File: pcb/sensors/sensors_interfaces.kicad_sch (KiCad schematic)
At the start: 23 parts, among them J3 CAN BUS, J4 DIMMER I2C, J5 DIMMER I2C, J6 FLOW HALL, J7 VALVE SSR, J8 BOILER SSR, Q2 AO3401A, Q3 2N7002, U4 TJA1051T/3, U5 TMP102AIDRLR

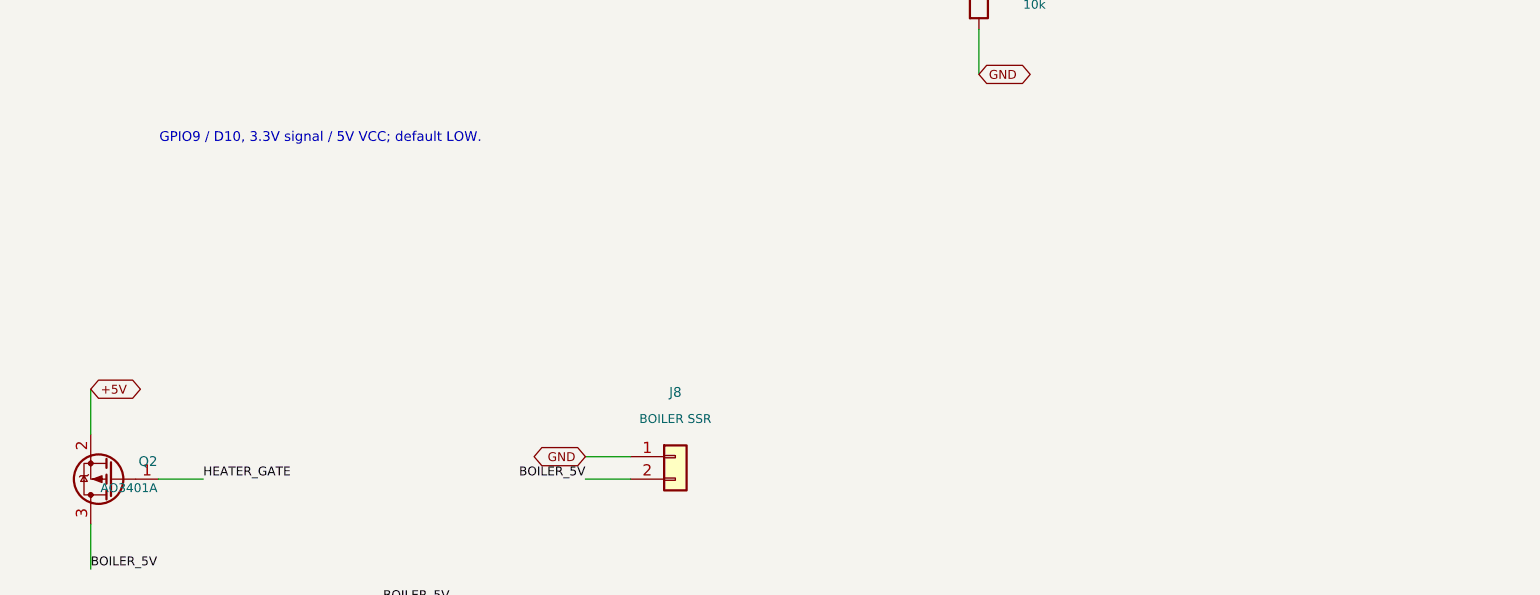
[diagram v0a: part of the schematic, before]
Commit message: Route the sensors board and add the accontrol and pressure inputs
Finish the sensors PCB routing. Give the XIAO a local footprint that keeps
only the header holes (1.0 mm drill) with one courtyard per header, so parts
can sit under the module.

Add J9 (XH 5, accontrol J1 order) with ZC on GPIO1 and DIM_CMD on GPIO3, and
an optional ADS1115 (U6, 0x49) with J10 and the screen_sensors pressure
filter. Record why the CAN terminator R12 is a 1206.

Co-Authored-By: Claude Opus 5.5 <noreply@anthropic.com>
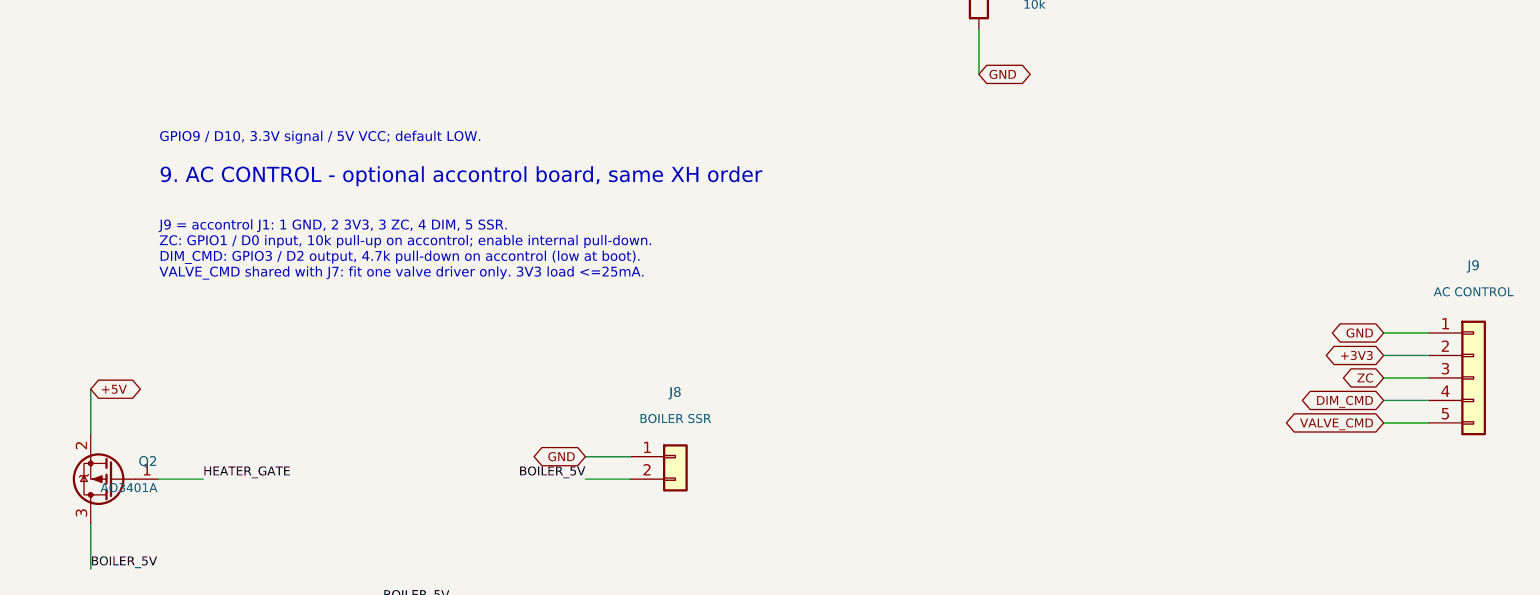
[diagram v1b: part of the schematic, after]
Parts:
- added J9: AC CONTROL, Connector_JST:JST_XH_B5B-XH-A_1x05_P2.50mm_Vertical, symbol Connector_Generic:Conn_01x05
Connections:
- net +3V3: now also J9.2 (Pin_2)
- net GND: now also J9.1 (Pin_1)
- net VALVE_CMD: now also J9.5 (Pin_5)
- new net DIM_CMD: J9.4 (Pin_4)
- new net ZC: J9.3 (Pin_3)
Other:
- note added: "9. AC CONTROL - optional accontrol board, same XH order"
- note added: "J9 = accontrol J1: 1 GND, 2 3V3, 3 ZC, 4 DIM, 5 SSR. ZC: GPIO1 / D0 input, 10k pull-up on accontrol; enable internal pull-down. DIM_CMD: GPIO3 / D2 output, 4.7k pull-down on accontrol (low at boot). VALVE_CMD shared with J7: fit one valve driver only. 3V3 load <=25mA."

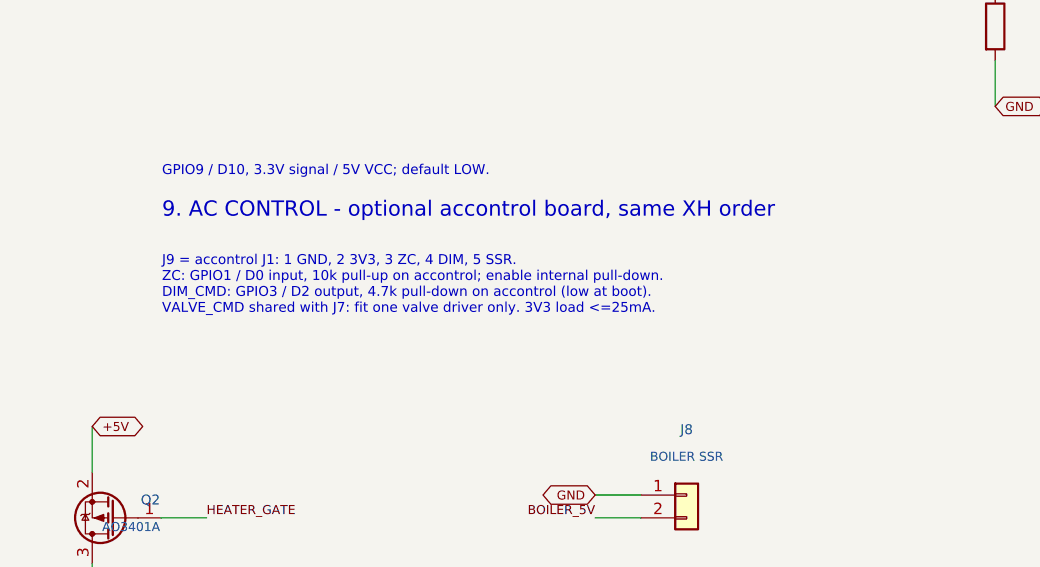
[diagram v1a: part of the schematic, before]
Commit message: Swap ZC and DIM_CMD on the XIAO to ease routing
DIM_CMD moves to GPIO1 (pin 1) and ZC to GPIO3 (pin 3). GPIO3 only acts as
a strapping pin once STRAP_JTAG_SEL is burned, so the ZC level at reset is
harmless; accontrol's pull-down still keeps DIM low during boot.

Co-Authored-By: Claude Opus 5.5 <noreply@anthropic.com>
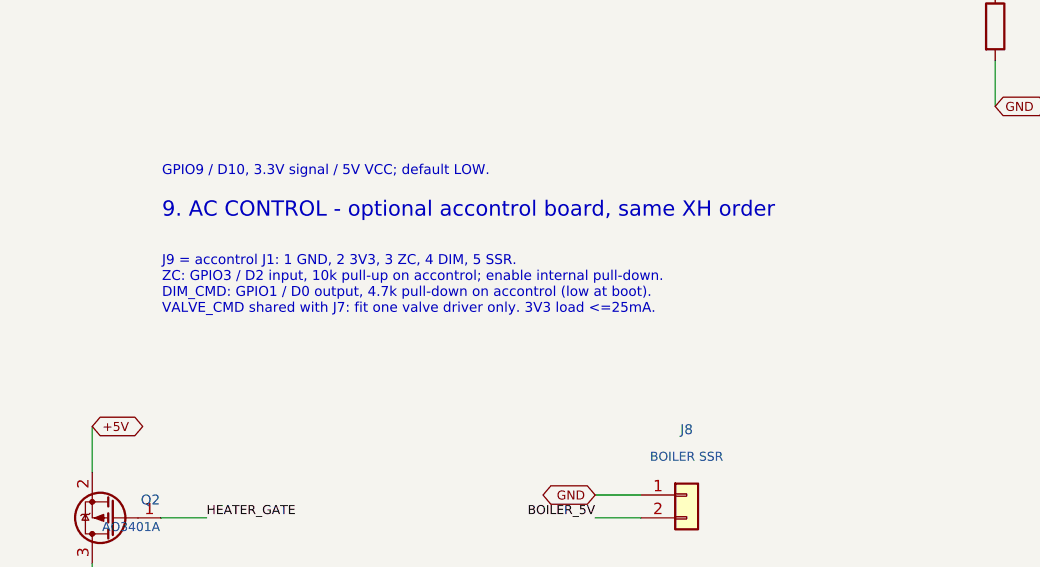
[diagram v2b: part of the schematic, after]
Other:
- note added: "J9 = accontrol J1: 1 GND, 2 3V3, 3 ZC, 4 DIM, 5 SSR. ZC: GPIO3 / D2 input, 10k pull-up on accontrol; enable internal pull-down. DIM_CMD: GPIO1 / D0 output, 4.7k pull-down on accontrol (low at boot). VALVE_CMD shared with J7: fit one valve driver only. 3V3 load <=25mA."
- note removed: "J9 = accontrol J1: 1 GND, 2 3V3, 3 ZC, 4 DIM, 5 SSR. ZC: GPIO1 / D0 input, 10k pull-up on accontrol; enable internal pull-down. DIM_CMD: GPIO3 / D2 output, 4.7k pull-down on accontrol (low at boot). VALVE_CMD shared with J7: fit one valve driver only. 3V3 load <=25mA."
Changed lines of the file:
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@@
 		)
 	)
-	(text "J9 = accontrol J1: 1 GND, 2 3V3, 3 ZC, 4 DIM, 5 SSR.\nZC: GPIO1 / D0 input, 10k pull-up on accontrol; enable internal pull-down.\nDIM_CMD: GPIO3 / D2 output, 4.7k pull-down on accontrol (low at boot).\nVALVE_CMD shared with J7: fit one valve driver only. 3V3 load <=25mA."
+	(text "J9 = accontrol J1: 1 GND, 2 3V3, 3 ZC, 4 DIM, 5 SSR.\nZC: GPIO3 / D2 input, 10k pull-up on accontrol; enable internal pull-down.\nDIM_CMD: GPIO1 / D0 output, 4.7k pull-down on accontrol (low at boot).\nVALVE_CMD shared with J7: fit one valve driver only. 3V3 load <=25mA."
 		(exclude_from_sim no)
 		(at 230 216 0)

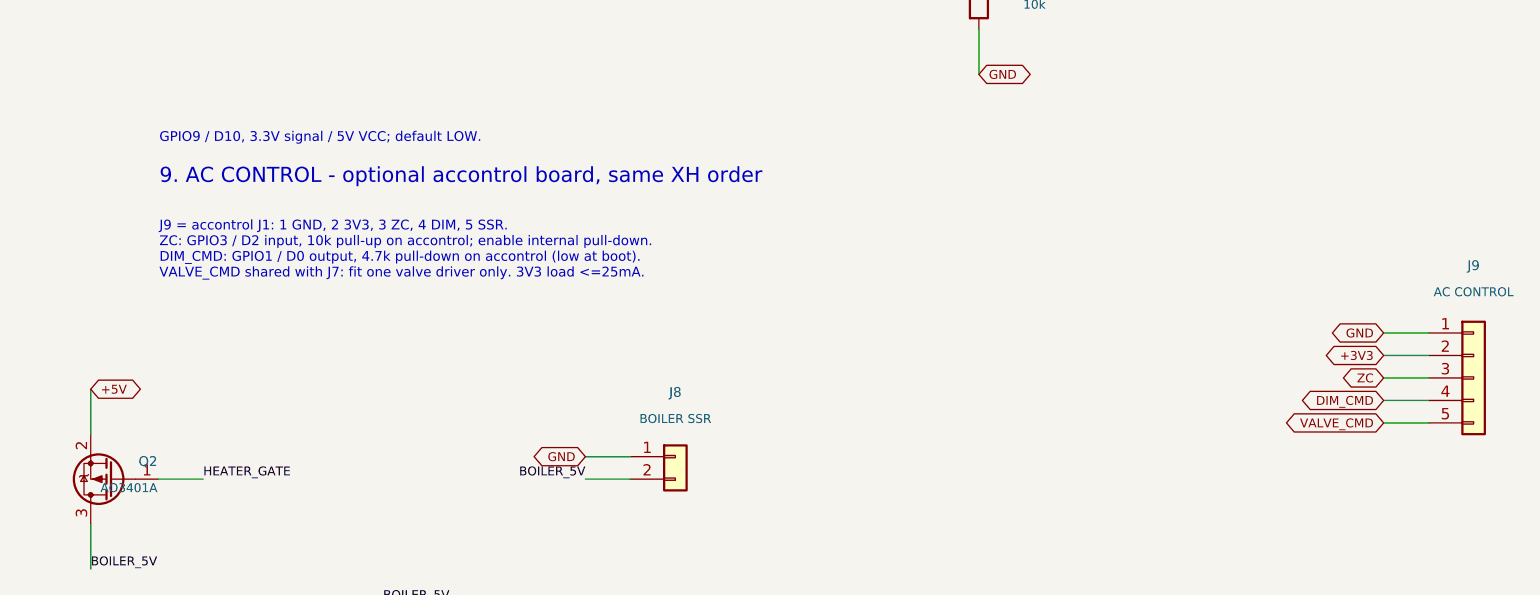
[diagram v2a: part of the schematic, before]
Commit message: Remove the accontrol connector J9 from the sensors board
The AC control board is shelved, so the valve and pump stay on the M5Stack
SSR (J7) and the RobotDyn dimmer (Grove I2C). Drop J9 and its wiring, and
leave D0/GPIO1 and D2/GPIO3 of the XIAO unconnected. The design notes say
how a future single AC board would take over from the dimmer I2C and J7.

The connectors now keep their J references on the PCB, hidden, with board
text labels for their functions.

Co-Authored-By: Claude Opus 5.5 <noreply@anthropic.com>
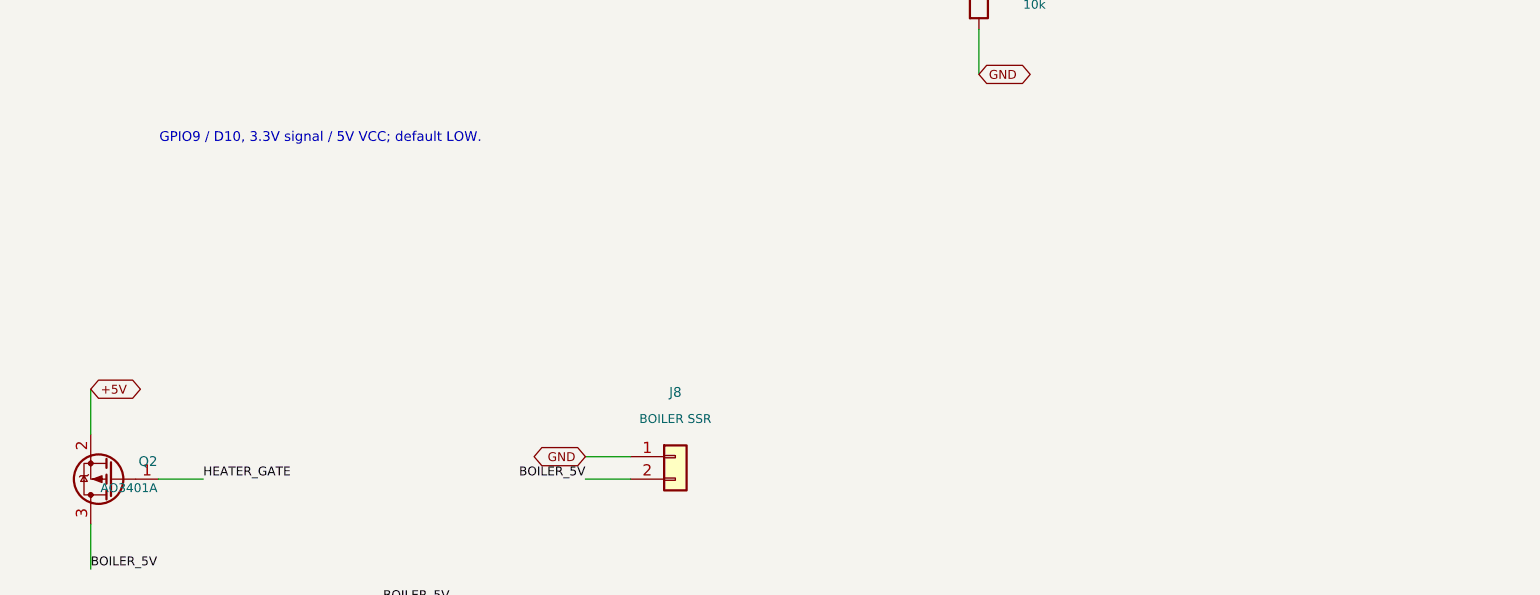
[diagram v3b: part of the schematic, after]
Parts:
- removed J9: AC CONTROL, Connector_JST:JST_XH_B5B-XH-A_1x05_P2.50mm_Vertical, symbol Connector_Generic:Conn_01x05
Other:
- note removed: "9. AC CONTROL - optional accontrol board, same XH order"
- note removed: "J9 = accontrol J1: 1 GND, 2 3V3, 3 ZC, 4 DIM, 5 SSR. ZC: GPIO3 / D2 input, 10k pull-up on accontrol; enable internal pull-down. DIM_CMD: GPIO1 / D0 output, 4.7k pull-down on accontrol (low at boot). VALVE_CMD shared with J7: fit one valve driver only. 3V3 load <=25mA."
